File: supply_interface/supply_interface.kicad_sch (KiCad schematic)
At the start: 33 parts, among them J1 39-28-1243, J10 MBES-152, J11 MBES-152, J12 MBES-152, J13 MBES-152, J2 39-28-1043, J3 MBES-152, J4 MBES-152, J5 282837-3, J6 MBES-152, J7 39-28-1043, J8 MBES-152, J9 MBES-152

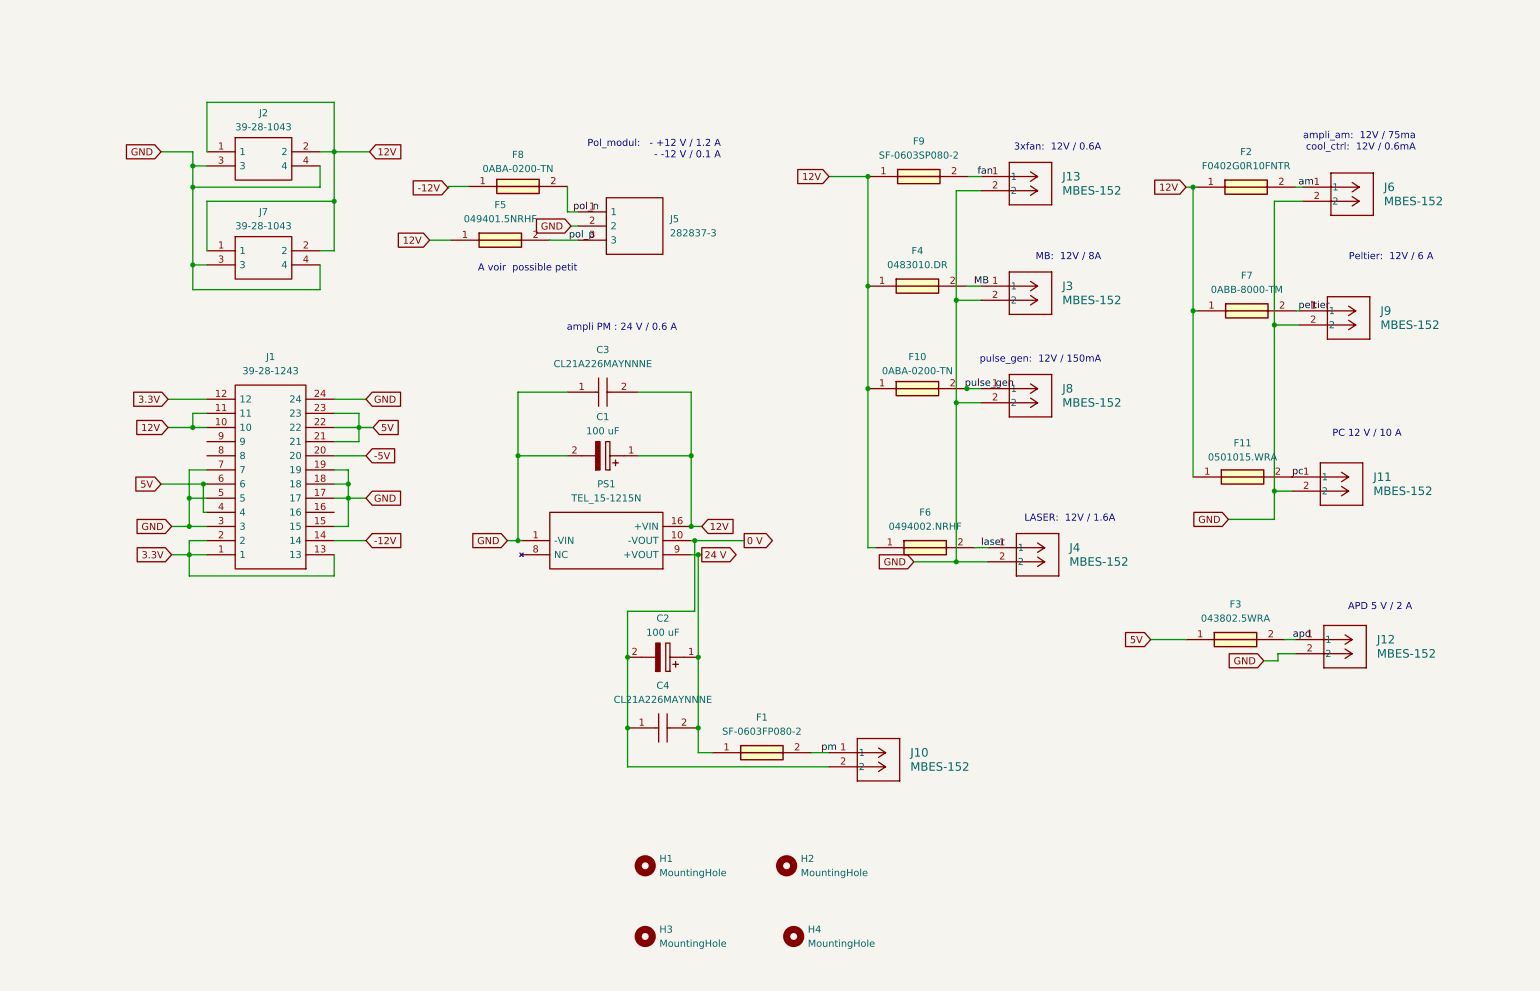
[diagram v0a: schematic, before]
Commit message: Add TVS protection and decoupling capacitors for power rails
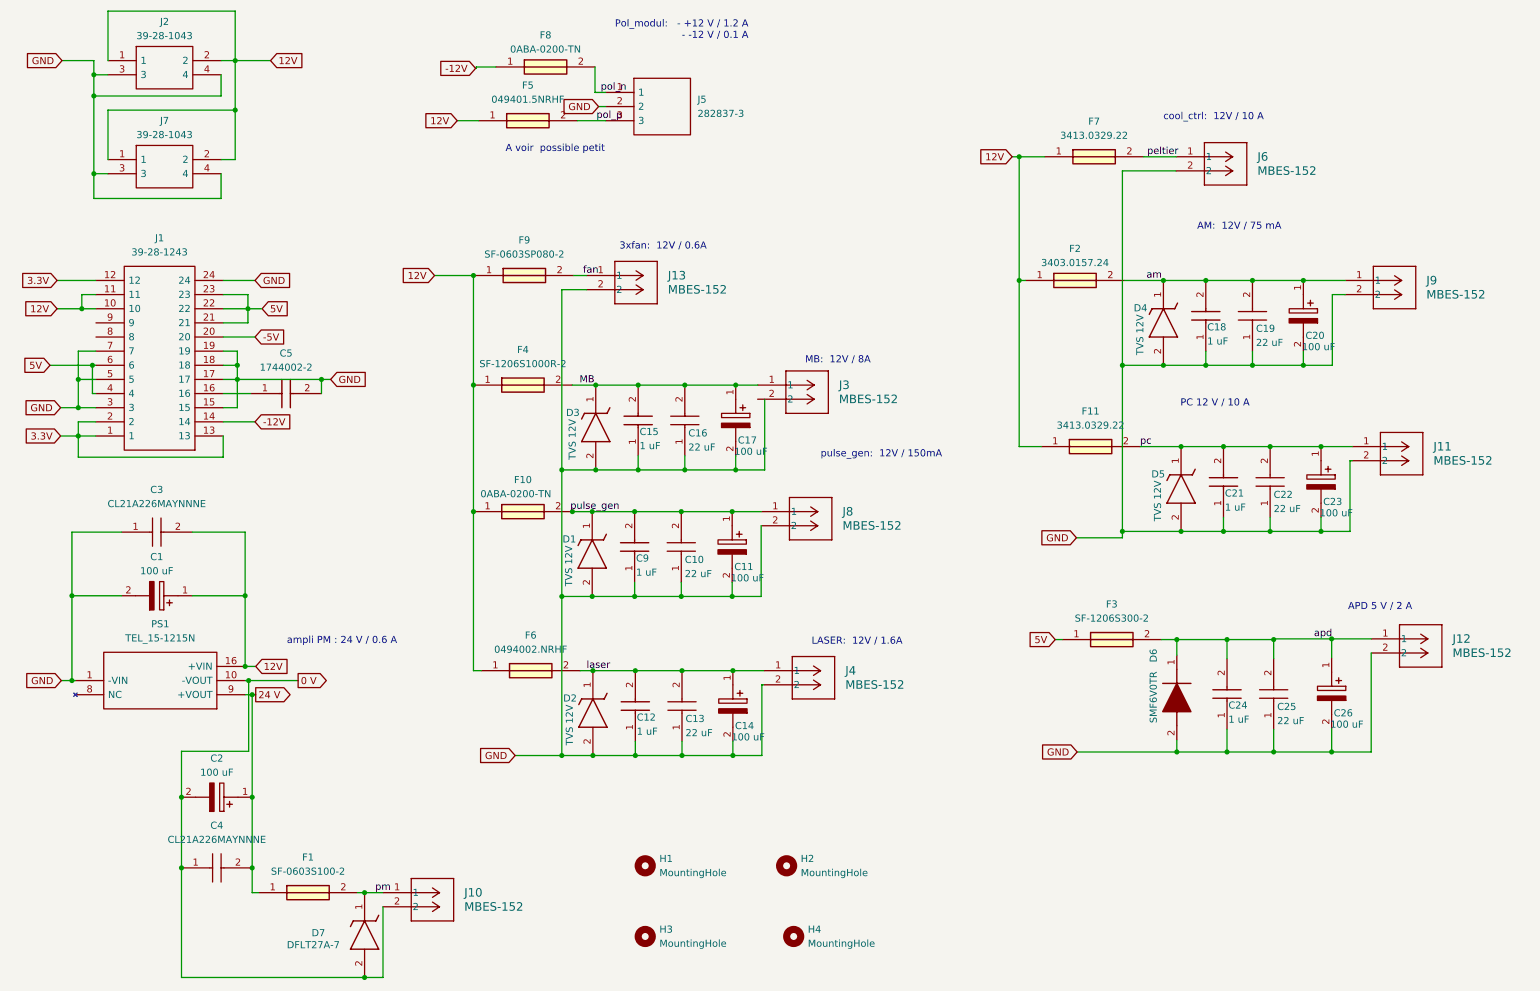
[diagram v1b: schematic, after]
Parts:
- removed F1: SF-0603FP080-2, FUSC1608X55N, symbol SF-0603FP080-2:SF-0603FP080-2
- removed F11: 0501015.WRA, FUSC3216X98N, symbol 0501015_WRA:0501015.WRA
- removed F2: F0402G0R10FNTR, F0402G0R10FNTR, symbol F0402G0R10FNTR:F0402G0R10FNTR
- removed F3: 043802.5WRA, FUSC1608X61N, symbol 043802_5WRA:043802.5WRA
- removed F4: 0483010.DR, FUSC3316X137N, symbol 0483010_DR:0483010.DR
- removed F7: 0ABB-8000-TM, 0ABB8000TM, symbol 0ABB-8000-TM:0ABB-8000-TM
- added C10, C13, C16, C19, C22, C25: 22 uF, CAPC2012X145N, symbol CL21A226MAYNNNE:CL21A226MAYNNNE
- added C11, C14, C17, C20, C23, C26: 100 uF, CAPPM7343X310N, symbol T55D107M025C0060:T55D107M025C0060
- added C12, C15, C18, C21, C24, C9: 1 uF, GRM15x, symbol GRM155R6YA105ME11J:GRM155R6YA105ME11J
- added C5: 1744002-2, 17440022, symbol 1744002-2:1744002-2
- added D1, D2, D3, D4, D5: TVS 12V, SODFL3718X130N, symbol ATV02W150-HF:ATV02W150-HF
- added D6: SMF6V0TR, SMF6V0TR, symbol SMF6V0TR:SMF6V0TR
- added D7: DFLT27A-7, DFLT27A7, symbol DFLT27A-7:DFLT27A-7
- added F1: SF-0603S100-2, FUSC1608X55N, symbol SF-0603S100-2:SF-0603S100-2
- added F11, F7: 3413.0329.22, FUSC3216X60N, symbol 3413.0329.22:3413.0329.22
- added F2: 3403.0157.24, 3403015724, symbol 3403.0157.24:3403.0157.24
- added F3: SF-1206S300-2, FUSC3116X70N, symbol SF-1206S300-2:SF-1206S300-2
- added F4: SF-1206S1000R-2, FUSC3216X90N, symbol SF-1206S1000R-2:SF-1206S1000R-2
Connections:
- net 0 V: now also D7.2 (A)
- net 12V: now also F11.1, F2.1, F4.1, F7.1
- net 24 V: now also F1.1
- net 5V: now also F3.1
- net GND: now also C10.1, C11.2, C12.1, C13.1, C14.2, C15.1, C16.1, C17.2, C18.1, C19.1, C20.2, C21.1, C22.1, C23.2, C24.1, C25.1, C26.2, C5.2, C9.1, D1.2 (A), D2.2 (A), D3.2 (A), D4.2 (A), D5.2 (A), D6.2 (A); no longer J3.2
- net MB: now also C15.2, C16.2, C17.1, D3.1 (K), F4.2
- net am: now also J9.1, C18.2, C19.2, C20.1, D4.1 (K), F2.2; no longer J6.1
- net apd: now also C24.2, C25.2, C26.1, D6.1 (K), F3.2
- net laser: now also C12.2, C13.2, C14.1, D2.1 (K)
- net pc: now also C21.2, C22.2, C23.1, D5.1 (K), F11.2
- net peltier: now also J6.1, F7.2; no longer J9.1
- net pm: now also D7.1 (K), F1.2
- net pulse_gen: now also C10.2, C11.1, C9.2, D1.1 (K)
- net at J1.16: now also C5.1
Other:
- note added: "AM: 12V / 75 mA"
- note added: "cool_ctrl: 12V / 10 A"
- note removed: "Peltier: 12V / 6 A"
- note removed: "ampli_am: 12V / 75ma cool_ctrl: 12V / 0.6mA"
- moved on the sheet: C1, C2, C3, C4, F10, F5, F6, F8, F9, J1, J10, J11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

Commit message: update2 ps_on connector
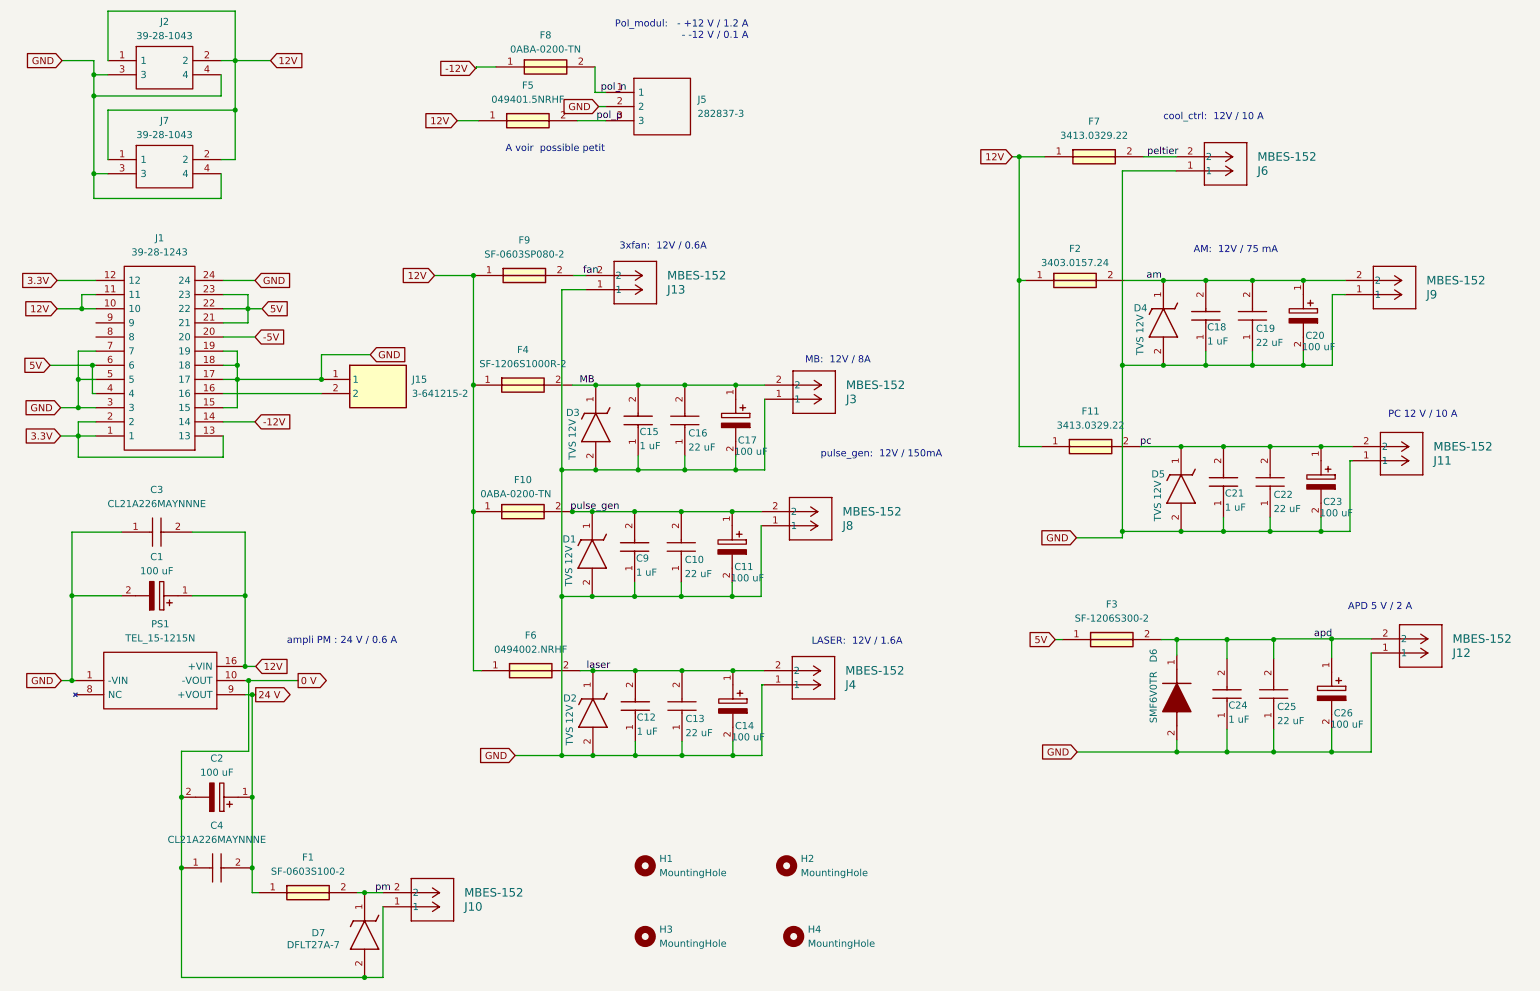
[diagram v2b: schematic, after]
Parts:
- removed C5: 1744002-2, 17440022, symbol 1744002-2:1744002-2
- added J15: 3-641215-2, SHDR2W66P0X254_1X2_508X572X813P, symbol 3-641215-2:3-641215-2
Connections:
- net 0 V: now also J10.1; no longer J10.2
- net GND: now also J11.1, J12.1, J13.1, J3.1, J4.1, J6.1, J8.1, J9.1, J15.1; no longer J11.2, J12.2, J13.2, J4.2, J6.2, J8.2, J9.2
- net MB: now also J3.2; no longer J3.1
- net am: now also J9.2; no longer J9.1
- net apd: now also J12.2; no longer J12.1
- net fan: now also J13.2; no longer J13.1
- net laser: now also J4.2; no longer J4.1
- net pc: now also J11.2; no longer J11.1
- net peltier: now also J6.2; no longer J6.1
- net pm: now also J10.2; no longer J10.1
- net pulse_gen: now also J8.2; no longer J8.1
- net at J1.16: now also J15.2
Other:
- moved on the sheet: J3
